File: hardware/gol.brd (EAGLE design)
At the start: 67.3 x 67.3 mm, 70 parts, among them J1 TC2050-IDC, J2 2057-MCR-B-S-RA-TSMT-NP-CS4-T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, U1 STM32F072CBT, U2 AP2111H-3.3TRG1SOT-223_DIO-M

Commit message: more routing.
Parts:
- moved R12 10.1 mm to (4.32, 14.7), turned to 270 degrees
- moved C5 0.25 mm to (19.1, 39.1)
- moved R15 0.25 mm to (21.1, 39.1)
- moved R16 0.25 mm to (23.1, 39.1)
- turned R2 to 0 degrees
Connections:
- net OUTA-L2: now also R3.1; no longer R2.1
- net OUTA-L3: now also R2.1; no longer R3.1
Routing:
- net NORTH: track 2.65 -> 91.9 mm, vias 0 -> 3
- net V+: track 195.8 -> 244.9 mm
- net EAST: track 18.9 -> 68.0 mm, vias 1 -> 4
- net OUTD14: track 9.63 -> 49.3 mm, vias 1 -> 5
- net OUTD13: track 6.08 -> 38.1 mm, vias 1 -> 2
- net N$5: track 0.00 -> 23.0 mm
- net N$6: track 0.00 -> 16.7 mm, vias 0 -> 3
- net OUTA-L3: track 3.79 -> 14.1 mm, vias 1 -> 3
- net OUTA-L2: track 4.97 -> 11.5 mm, vias 1 -> 3
- net OUTA-L1: track 6.55 -> 12.8 mm, vias 1 -> 3
- net N$18: track 0.00 -> 6.24 mm
- net N$19: track 0.00 -> 4.53 mm
- net IN_ROW2: track 58.6 -> 62.6 mm
- net BOOT0: track 34.3 -> 36.8 mm
- net N$1: track 9.94 -> 11.3 mm
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
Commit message: More routing.
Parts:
- turned BTN18 to 180 degrees
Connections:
- net OUTA-L1: now also R3.1; no longer R1.1
- net OUTA-L2: now also R1.1; no longer R3.1
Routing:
- net OUTA-L1: track 12.8 -> 76.9 mm, vias 3 -> 9
- net N$4: track 0.00 -> 50.7 mm
- net PB15: track 16.3 -> 47.2 mm, vias 1 -> 5
- net GND: track 288.8 -> 319.1 mm, vias 7 -> 9
- net OUTA-L2: track 11.5 -> 38.6 mm, vias 3 -> 5
- net N$5: track 23.0 -> 39.9 mm
- net N$6: track 16.7 -> 32.1 mm
- net V+: track 244.9 -> 251.1 mm
- net IN_COL1: track 63.8 -> 65.3 mm
- net IN_COL0: track 57.9 -> 59.1 mm
- net N$1: track 11.3 -> 12.2 mm
- net ROW2: track 10.3 -> 11.2 mm
- net COL0: track 10.8 -> 11.5 mm
- net OUTA-L3: track 14.1 -> 13.5 mm
- net IN_ROW2: track 62.6 -> 63.2 mm

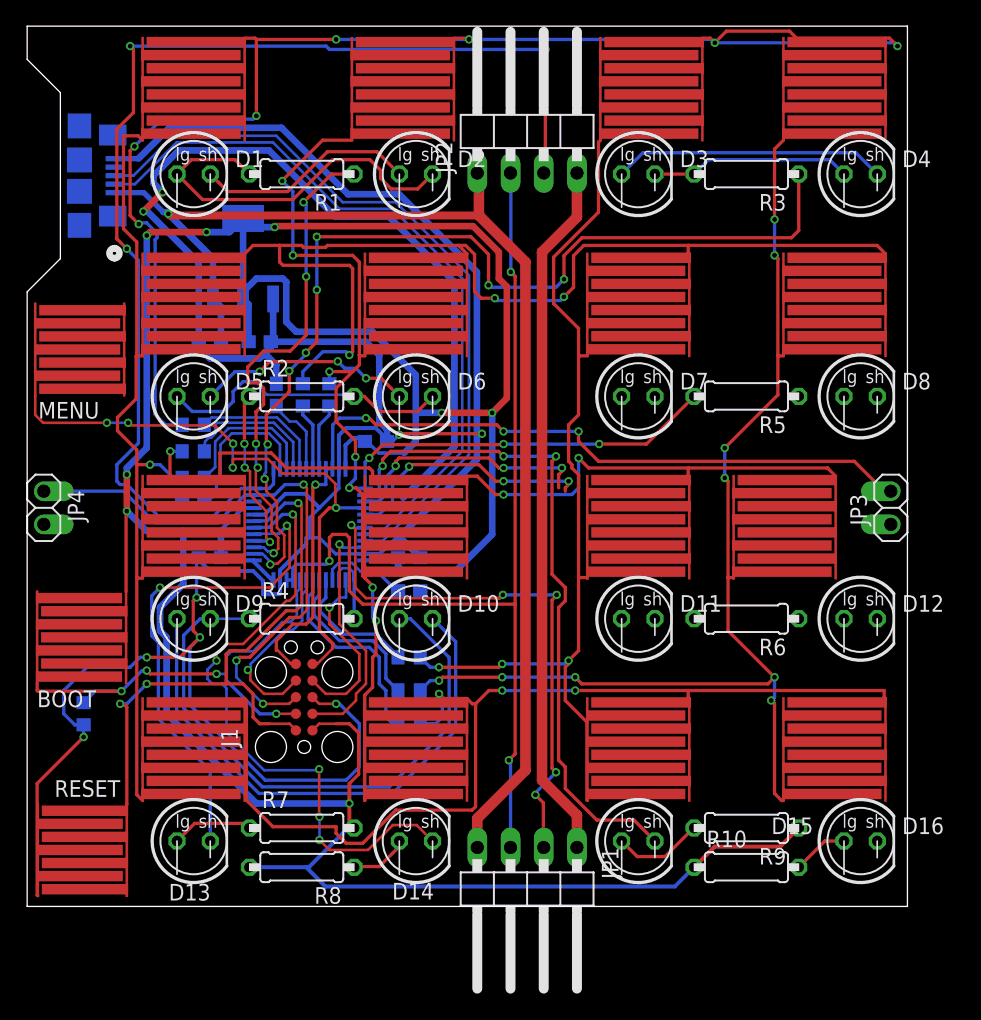
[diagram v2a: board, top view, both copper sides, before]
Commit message: Finishes routing most of the LEDs.
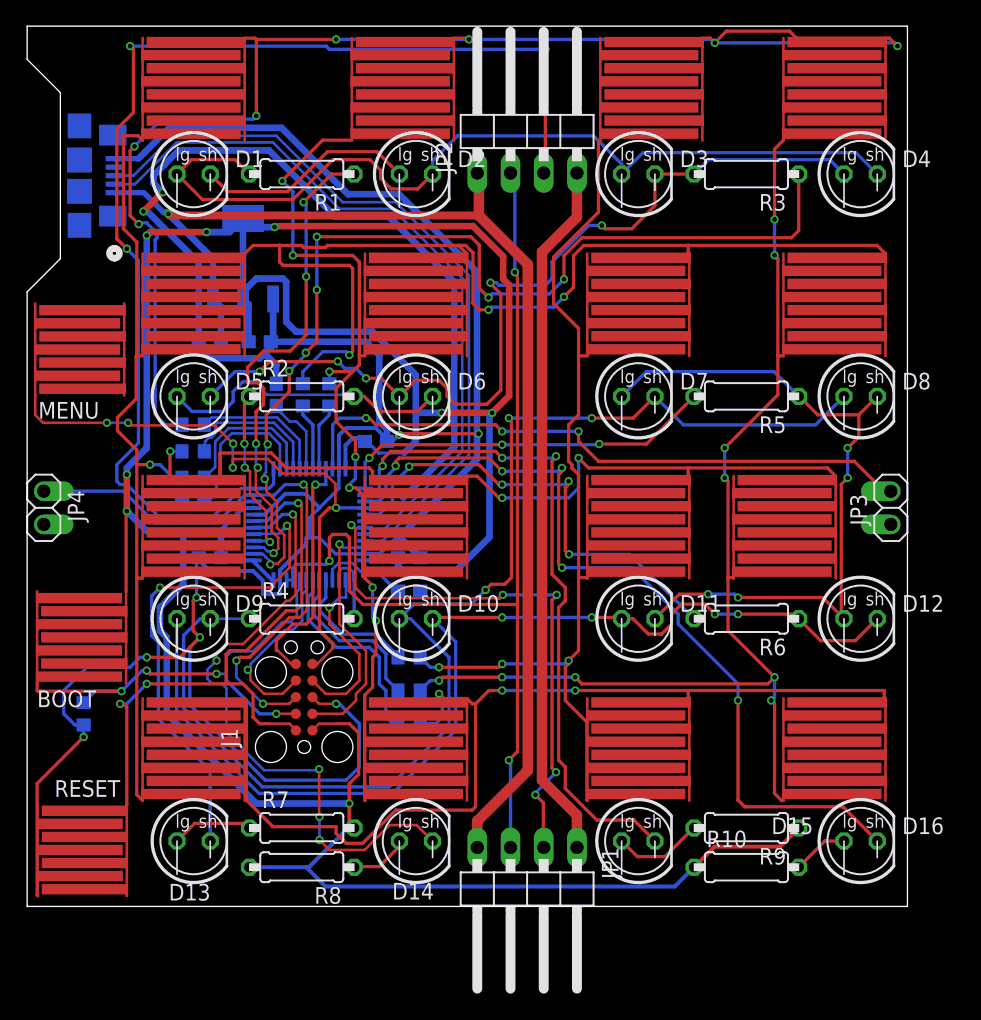
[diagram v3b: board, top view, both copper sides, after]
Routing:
- net N$14: track 0.00 -> 54.5 mm, vias 0 -> 4
- net N$13: track 46.2 -> 96.4 mm, vias 0 -> 3
- net OUTD16: track 19.4 -> 64.3 mm, vias 3 -> 5
- net N$15: track 42.3 -> 80.1 mm, vias 0 -> 4
- net N$6: track 32.1 -> 69.0 mm, vias 3 -> 5
- net N$4: track 50.7 -> 68.6 mm
- net OUTB-L3: track 19.3 -> 36.1 mm, vias 3 -> 4
- net OUTA-L1: track 76.9 -> 78.1 mm
- net IN_ROW1: track 76.8 -> 78.0 mm
- net GND: track 319.1 -> 318.6 mm

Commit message: Fixes routing of missing gnd lines.
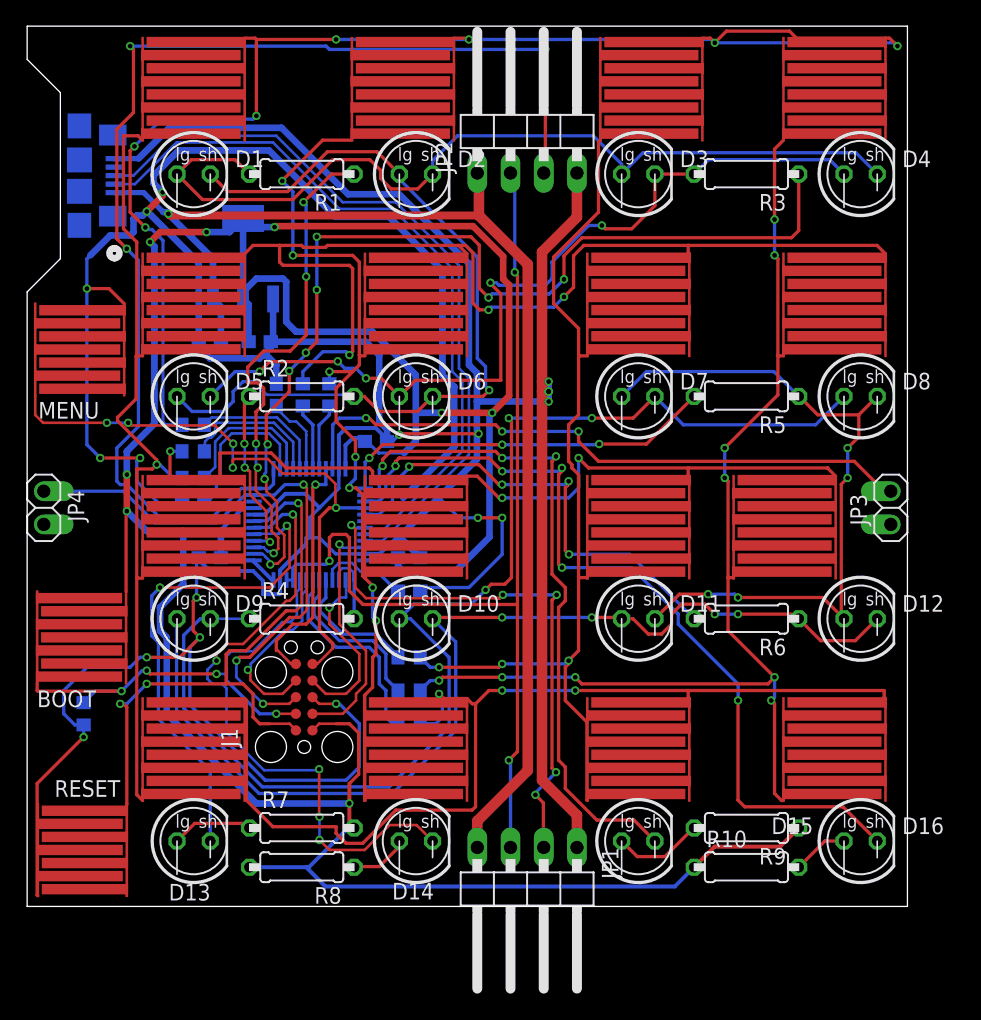
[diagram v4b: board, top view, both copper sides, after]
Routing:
- net GND: track 318.6 -> 377.3 mm, vias 9 -> 18
- net N$5: track 39.9 -> 63.8 mm, vias 0 -> 1
- net N$6: track 69.0 -> 66.7 mm
- net IN_ROW0: track 108.0 -> 107.4 mm

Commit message: Adds 4-pin connector to east and west as well. Routes all remaining airwires.
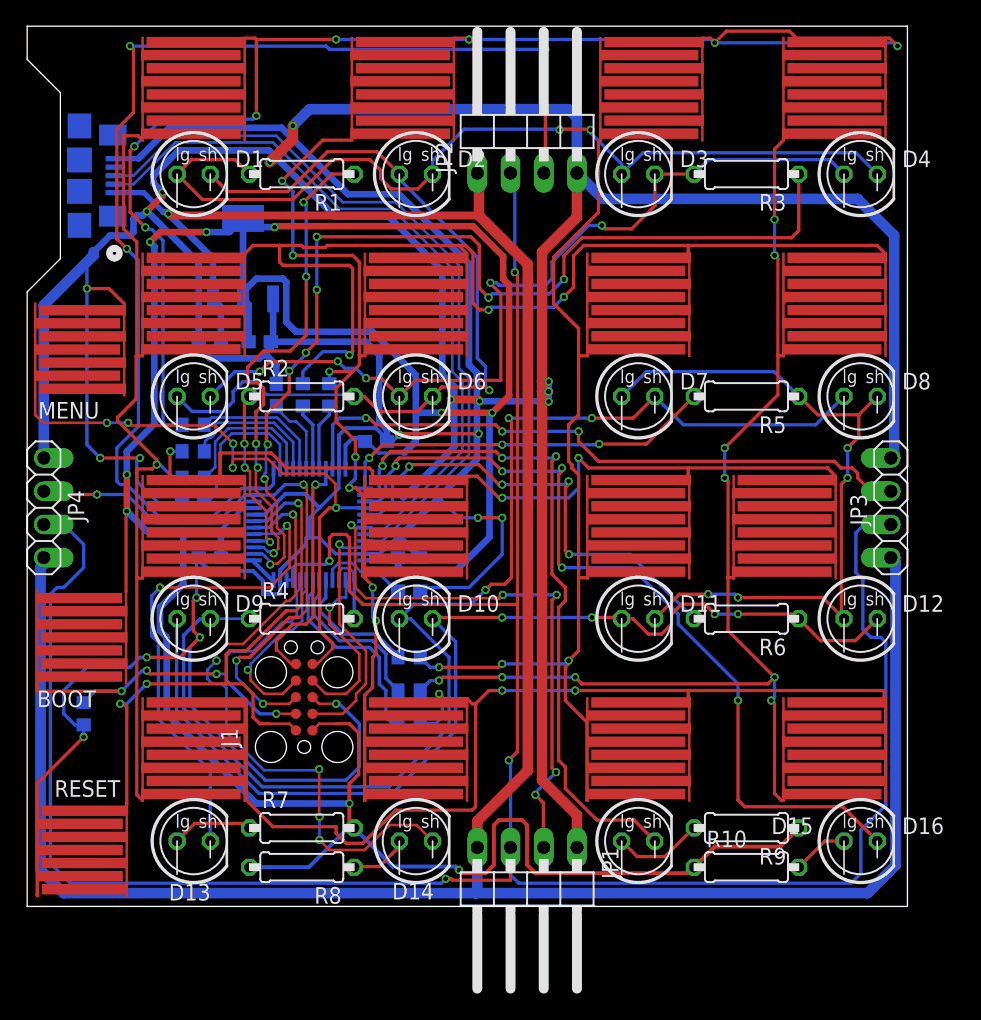
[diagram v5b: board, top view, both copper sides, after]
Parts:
- JP3, JP4: device parts:1X02 -> parts:1X04
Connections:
- removed net +12V: JP3.1, JP4.2
- net +5V: now also JP3.1, JP4.4
- net CAN_TR: now also JP3.2, JP4.3
- net EAST: now also JP3.3; no longer JP3.2
- net GND: now also JP3.4, JP4.1
- net WEST: now also JP4.2; no longer JP4.1
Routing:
- net CAN_TR: track 77.4 -> 206.0 mm, vias 3 -> 4
- net +5V: track 94.8 -> 213.0 mm
- net GND: track 377.3 -> 471.5 mm, vias 18 -> 22
- net V+: track 251.1 -> 254.8 mm, vias 8 -> 9
- net N$4: track 68.6 -> 69.3 mm, vias 0 -> 2
- net WEST: vias 3 -> 4

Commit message: Places parts labels on top and bottom layer.
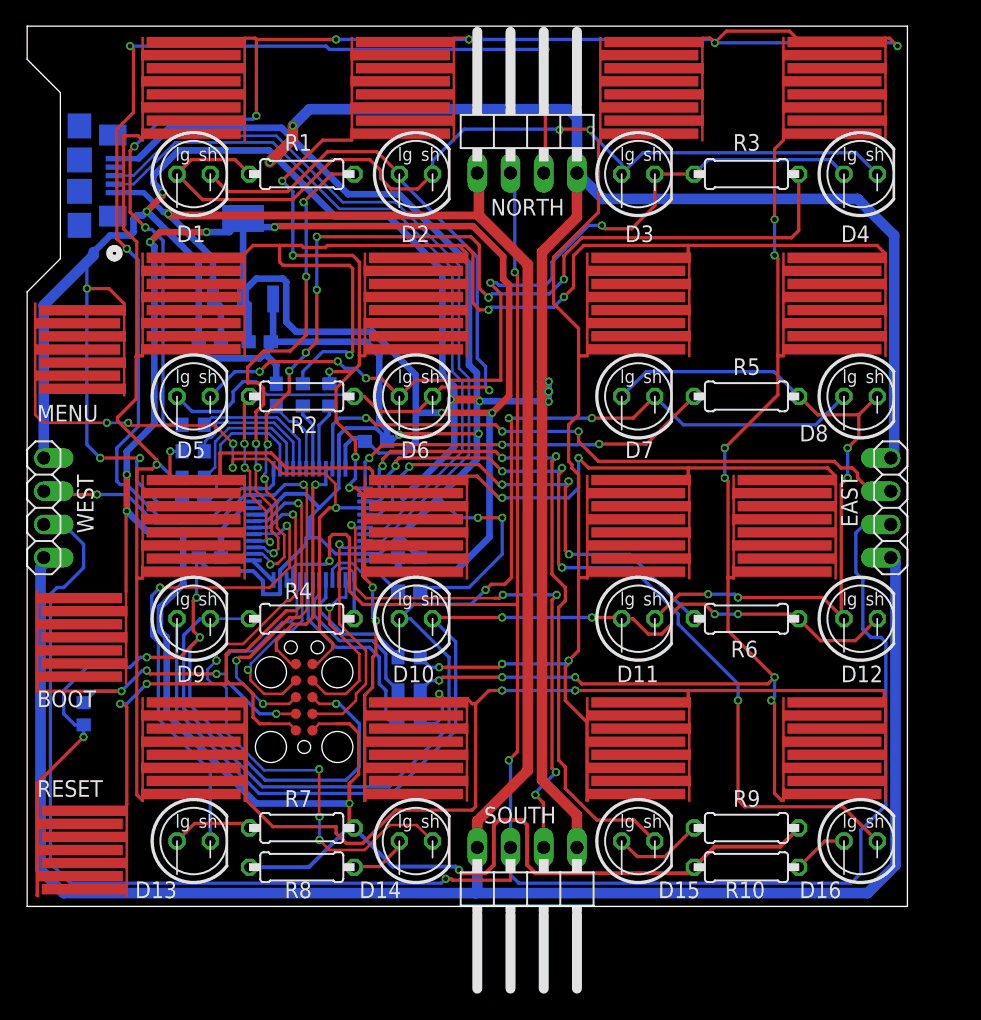
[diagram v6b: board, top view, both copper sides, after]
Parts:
- renumbered JP1 to SOUTH, JP2 to NORTH, JP3 to EAST, JP4 to WEST

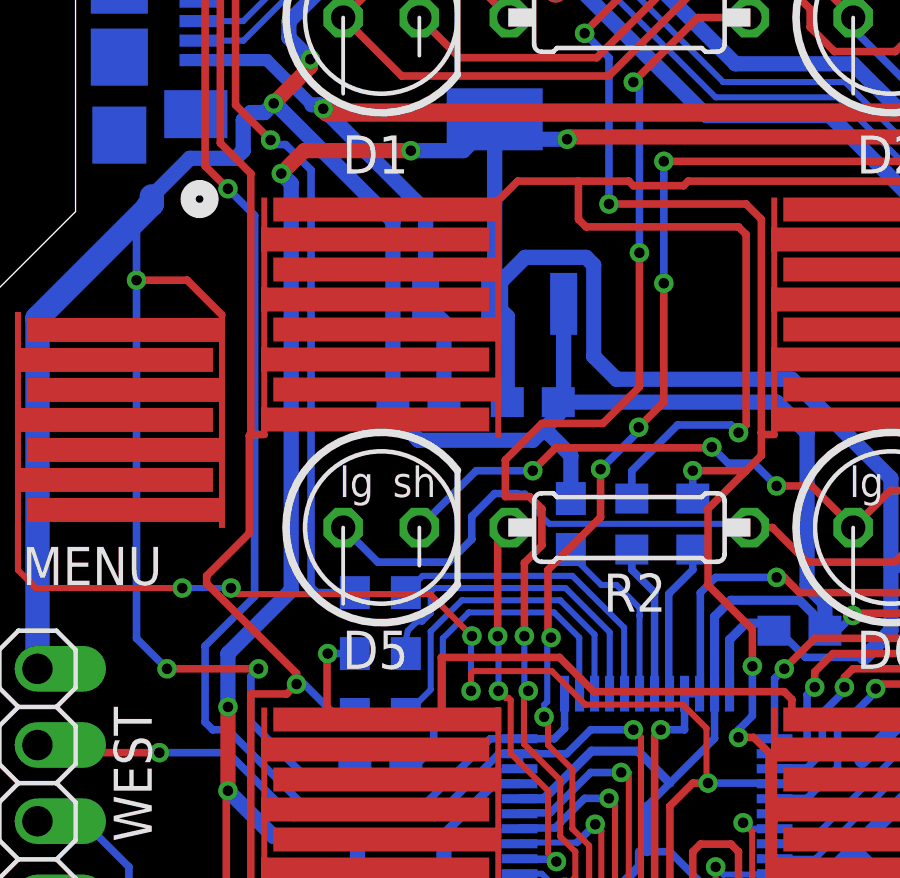
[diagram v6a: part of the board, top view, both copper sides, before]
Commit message: more labeling work. Updates parts so that they have outlines.
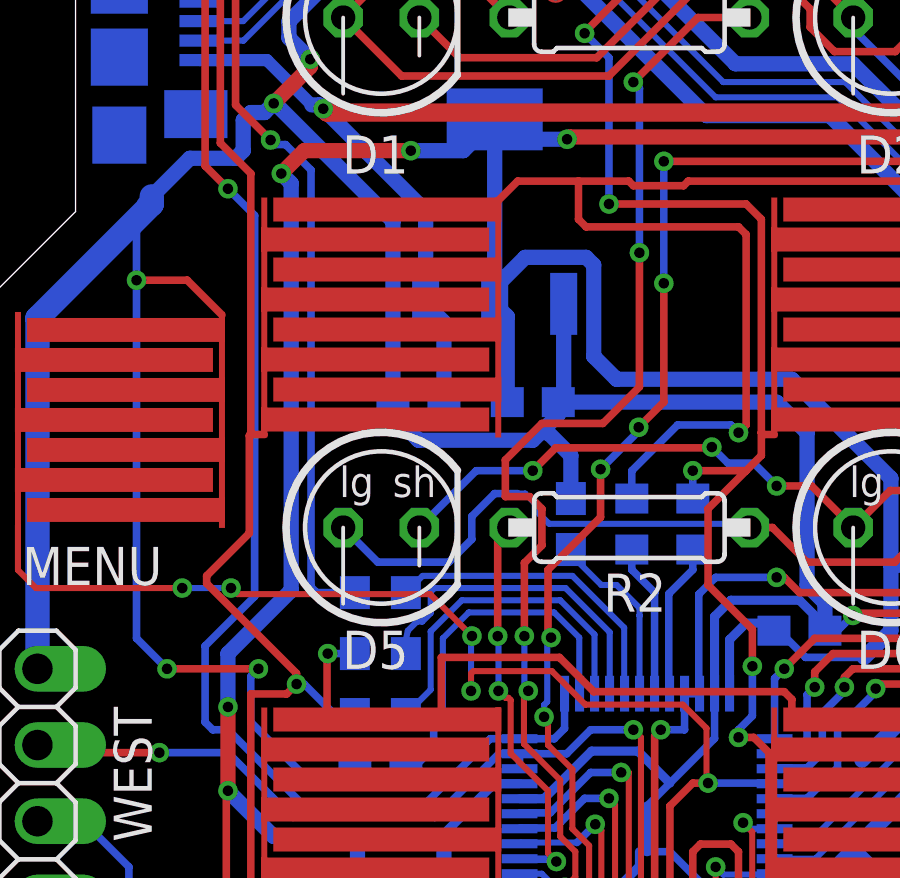
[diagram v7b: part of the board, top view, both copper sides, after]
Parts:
- R12: value 1M -> 470k

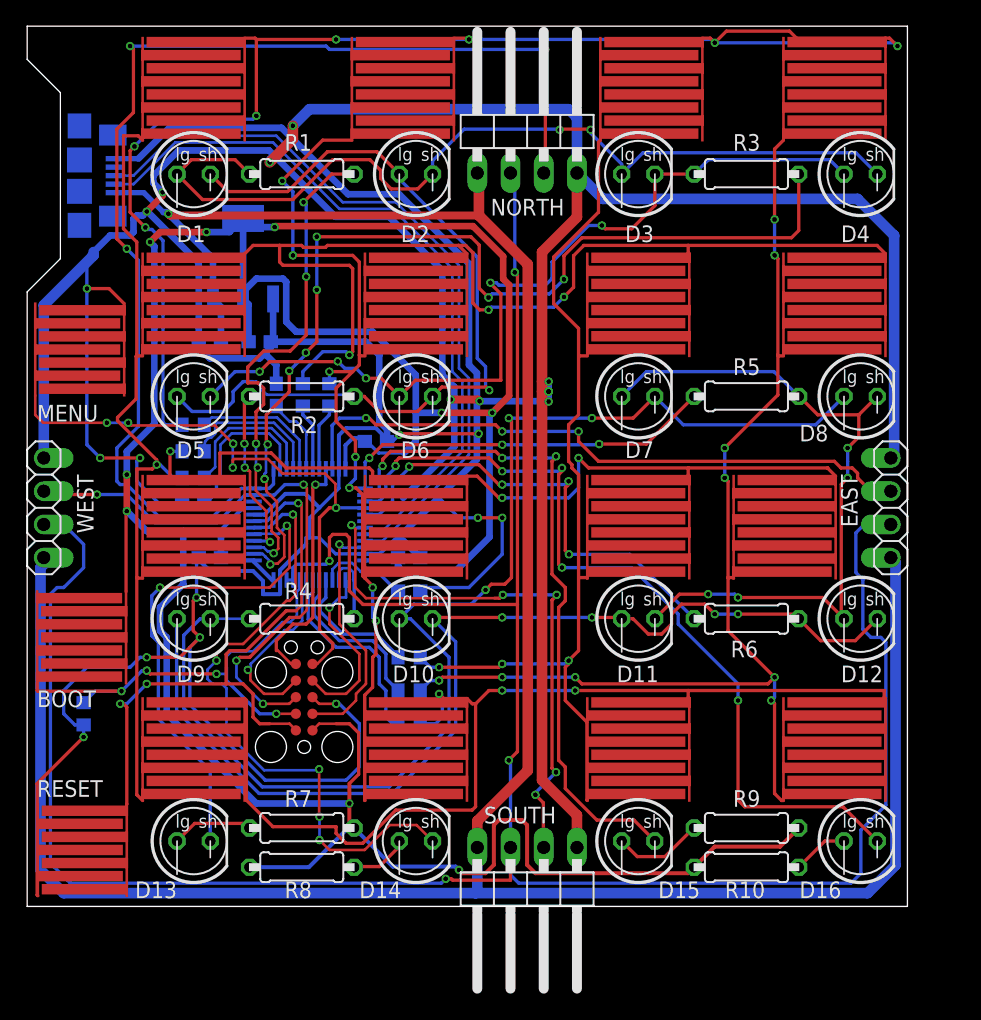
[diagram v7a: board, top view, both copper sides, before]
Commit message: Adds ground pour and vias.
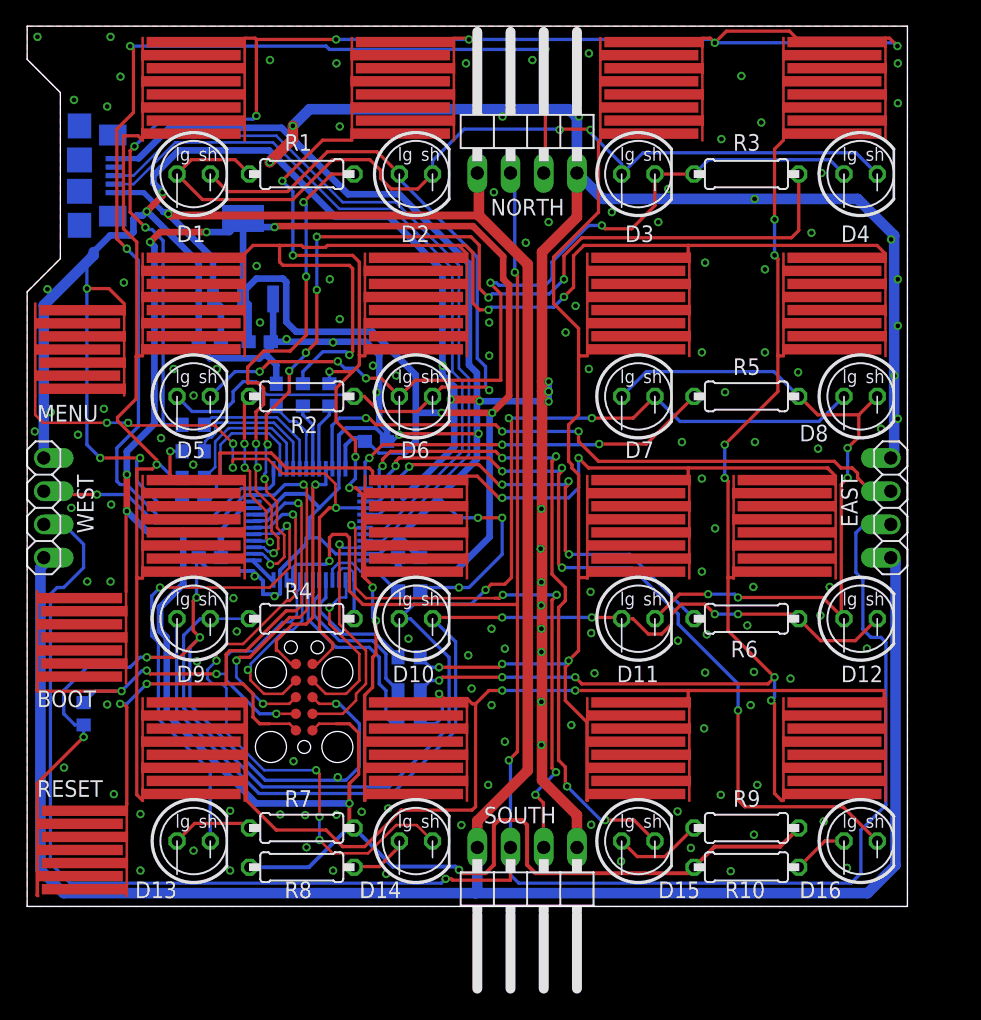
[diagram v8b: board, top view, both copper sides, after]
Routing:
- net OUTD15: track 52.4 -> 52.5 mm, vias 3 -> 5
- net GND: vias 22 -> 164
- added copper zone on layer 1, net GND
- added copper zone on layer 16, net GND
